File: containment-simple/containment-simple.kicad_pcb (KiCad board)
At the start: 2 copper layers, 20 x 20 mm, 0 parts

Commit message: containment simple mostly done
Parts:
- added C1: .1uF, Capacitor_SMD:C_0603_1608Metric, F.Cu at (125.2, 103.9)
- added C3: 10uF, Capacitor_SMD:C_1206_3216Metric, F.Cu at (139.2, 86.9)
- added D1: LED, LED_SMD:LED_1206_3216Metric, F.Cu at (140.5, 90.7)
- added D2: D, Diode_SMD:D_SOD-123, B.Cu at (134.9, 83.1)
- added D3: LED, LED_SMD:LED_1206_3216Metric, F.Cu at (134.9, 83.1)
- added D4: D, Diode_SMD:D_SOD-123, B.Cu at (129.8, 85.6)
- added D5: LED, LED_SMD:LED_1206_3216Metric, F.Cu at (129.8, 85.6)
- added D6: D, Diode_SMD:D_SOD-123, B.Cu at (125.7, 89.7)
- added D7: LED, LED_SMD:LED_1206_3216Metric, F.Cu at (125.7, 89.4)
- added D8: D, Diode_SMD:D_SOD-123, B.Cu at (123.2, 94.7)
- added D9: LED, LED_SMD:LED_1206_3216Metric, F.Cu at (123.2, 95.0)
- added H1: MountingHole_Pad, Containment:MountingHole_2-56_ExtraClearance, F.Cu at (140.0, 82.0)
- added H2: MountingHole_Pad, Containment:MountingHole_2-56_ExtraClearance, F.Cu at (122.0, 100.0)
- added H3: MountingHole_Pad, Containment:MountingHole_2-56_ExtraClearance, F.Cu at (140.0, 118.0)
- added H4: MountingHole_Pad, Containment:MountingHole_2-56_ExtraClearance, F.Cu at (158.0, 100.0)
- added J1: Conn_02x05_Odd_Even, Connector_PinHeader_2.54mm:PinHeader_2x05_P2.54mm_Vertical, F.Cu at (141.3, 105.1)
- added J3: Conn_01x02, Connector_PinHeader_2.54mm:PinHeader_1x02_P2.54mm_Vertical, F.Cu at (132.8, 80.5)
- added J4: Conn_01x02, Connector_PinHeader_2.54mm:PinHeader_1x02_P2.54mm_Vertical, F.Cu at (127.0, 83.8)
- added J5: Conn_01x02, Connector_PinHeader_2.54mm:PinHeader_1x02_P2.54mm_Vertical, F.Cu at (122.4, 88.9)
- added J6: Conn_01x02, Connector_PinHeader_2.54mm:PinHeader_1x02_P2.54mm_Vertical, F.Cu at (119.9, 95.2)
- added JTEMP1: Conn_01x02, Connector_PinHeader_2.54mm:PinHeader_1x02_P2.54mm_Vertical, F.Cu at (120.4, 106.9)
- added Q1: BSS84, Package_TO_SOT_SMD:SOT-23, F.Cu at (134.6, 93.0)
- added Q2: BSS84, Package_TO_SOT_SMD:SOT-23, F.Cu at (133.9, 96.8)
- added Q3: BSS84, Package_TO_SOT_SMD:SOT-23, F.Cu at (130.3, 96.8)
- added Q4: BSS84, Package_TO_SOT_SMD:SOT-23, F.Cu at (126.5, 96.8)
- added R1: 1k, Resistor_SMD:R_1206_3216Metric, F.Cu at (137.9, 90.7)
- added R2: 1k, Resistor_SMD:R_1206_3216Metric, F.Cu at (135.4, 88.6)
- added R3: 1k, Resistor_SMD:R_1206_3216Metric, F.Cu at (131.8, 88.4)
- added R4: 1k, Resistor_SMD:R_1206_3216Metric, F.Cu at (131.3, 92.5)
- added R5: 1k, Resistor_SMD:R_1206_3216Metric, F.Cu at (128.5, 92.5)
- added U1: TMP411, Package_SO:SOIC-8_3.9x4.9mm_P1.27mm, B.Cu at (130.0, 104.1)
- added U2: PCA9557, Package_SO:SOIC-16_3.9x9.9mm_P1.27mm, F.Cu at (131.4, 103.0)
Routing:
- net GND: track 0.00 -> 29.5 mm
- net +5V: track 0.00 -> 23.8 mm, vias 0 -> 1
- net Net-(D6-Pad1): track 0.00 -> 21.2 mm
- net Net-(D4-Pad1): track 0.00 -> 20.0 mm
- net scl: track 0.00 -> 18.6 mm, vias 0 -> 1
- net Net-(D2-Pad1): track 0.00 -> 18.0 mm
- net /p4: track 0.00 -> 17.6 mm
- net sda: track 0.00 -> 16.0 mm, vias 0 -> 1
- net +12V: track 0.00 -> 15.7 mm
- net Net-(D8-Pad1): track 0.00 -> 14.5 mm
- net Net-(JTEMP1-Pad2): track 0.00 -> 8.24 mm
- net Net-(JTEMP1-Pad1): track 0.00 -> 8.07 mm
- net Net-(D7-Pad2): track 0.00 -> 7.32 mm
- net Net-(D9-Pad2): track 0.00 -> 6.04 mm
- net Net-(D3-Pad2): track 0.00 -> 4.60 mm
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- added copper zone on B.Cu, net +5V
- added copper zone on F.Cu, net GND
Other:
- board size 20 x 20 mm -> 45.7 x 45.7 mm

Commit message: some lcsc stuff
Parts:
- added R6: 10k, Resistor_SMD:R_1206_3216Metric, B.Cu at (133.5, 96.2)
- added R7: 10k, Resistor_SMD:R_1206_3216Metric, B.Cu at (133.5, 99.5)
- added R8: 10k, Resistor_SMD:R_1206_3216Metric, B.Cu at (127.9, 96.2)
- added R9: 10k, Resistor_SMD:R_1206_3216Metric, B.Cu at (127.9, 99.5)

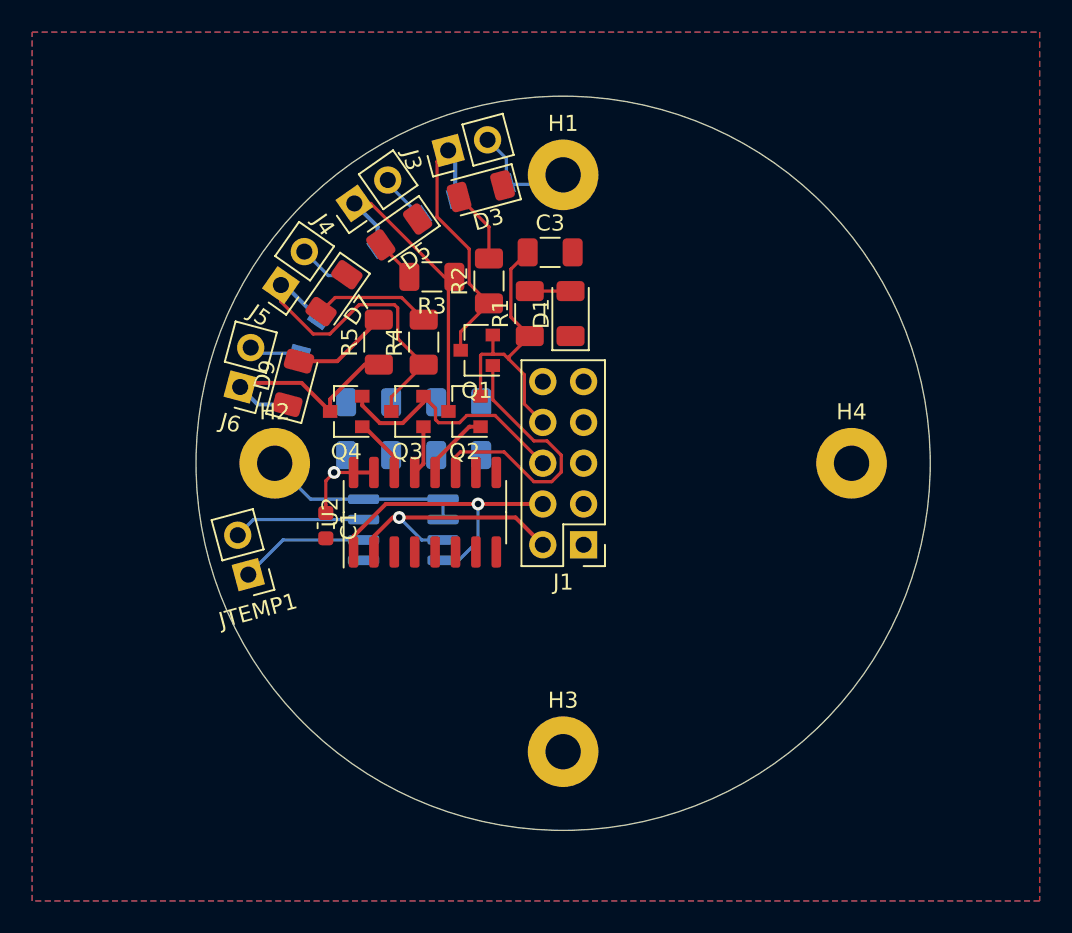
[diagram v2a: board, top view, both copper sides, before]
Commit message: more lcsc, redo a lot of inner containment
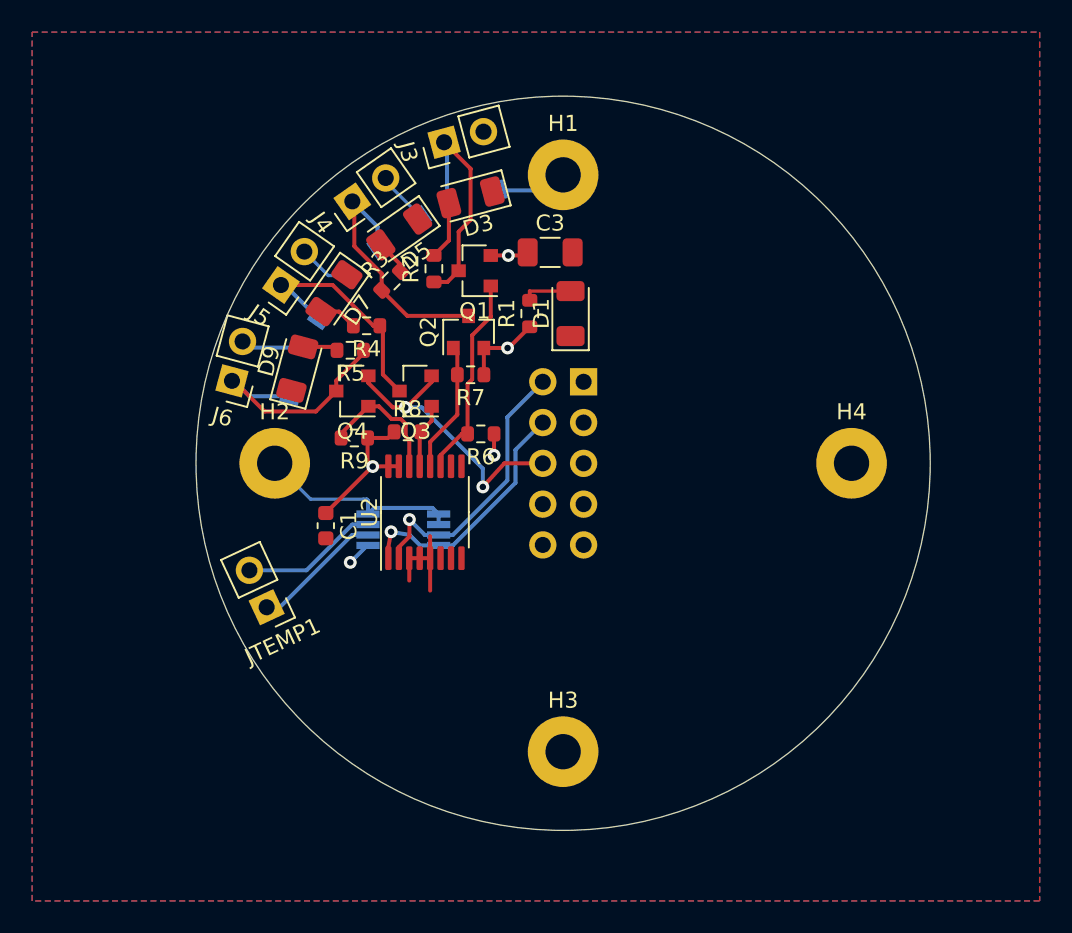
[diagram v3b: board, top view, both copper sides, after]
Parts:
- J1: moved to B.Cu
- R1, R2, R3, R4, R5: footprint Resistor_SMD:R_1206_3216Metric -> Resistor_SMD:R_0603_1608Metric
- R6, R7, R8, R9: footprint Resistor_SMD:R_1206_3216Metric -> Resistor_SMD:R_0603_1608Metric; moved to F.Cu
- U1: footprint Package_SO:SOIC-8_3.9x4.9mm_P1.27mm -> Package_SO:VSSOP-8_3.0x3.0mm_P0.65mm
- U2: footprint Package_SO:SOIC-16_3.9x9.9mm_P1.27mm -> Package_SO:TSSOP-16_4.4x5mm_P0.65mm
- moved J1 10.2 mm to (141.3, 94.9)
- moved R7 5.06 mm to (134.2, 94.5)
- moved Q2 4.96 mm to (134.1, 91.8), turned to 90 degrees
- moved Q1 4.95 mm to (134.5, 88.0)
- moved R4 3.70 mm to (127.8, 91.4), turned to 180 degrees
- moved R2 3.51 mm to (132.0, 87.9)
- moved R8 3.04 mm to (130.3, 98.0), turned to 0 degrees
- moved R3 2.55 mm to (129.3, 88.6), turned to 45 degrees
- moved R6 2.40 mm to (134.9, 98.2)
- moved JTEMP1 2.33 mm to (121.5, 109.0), turned to 205 degrees
- moved R5 1.85 mm to (126.7, 93.0), turned to 180 degrees
- moved R9 1.39 mm to (127.0, 98.4)
- moved Q3 1.37 mm to (130.8, 95.5)
- moved Q4 1.33 mm to (126.9, 95.5)
- moved D9 0.92 mm to (123.4, 94.1)
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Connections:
- R6 pad 2: /p0 -> /p4
- R7 pad 2: /p1 -> /p5
- R8 pad 2: /p2 -> /p6
- R9 pad 2: /p3 -> /p7
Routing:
- net Net-(D6-Pad1): track 21.2 -> 15.0 mm
- net Net-(D7-Pad2): track 7.32 -> 2.38 mm
- net /p4: track 17.6 -> 12.7 mm
- net Net-(D4-Pad1): track 20.0 -> 15.5 mm
- net /p7: track 3.75 -> 8.18 mm
- net +5V: track 23.8 -> 19.8 mm, vias 1 -> 5
- net GND: track 29.5 -> 33.5 mm
- net Net-(D9-Pad2): track 6.04 -> 2.20 mm
- net /p5: track 4.43 -> 8.17 mm
- net Net-(D2-Pad1): track 18.0 -> 14.8 mm
- net scl: track 18.6 -> 15.8 mm
- net +12V: track 15.7 -> 18.1 mm, vias 0 -> 2
- net sda: track 16.0 -> 17.6 mm
- net /p6: track 3.07 -> 4.04 mm
- net Net-(D3-Pad2): track 4.60 -> 3.64 mm
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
